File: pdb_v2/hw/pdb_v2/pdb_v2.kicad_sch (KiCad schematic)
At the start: 73 parts, among them J1 XT30-M_Ver, J2 JST-PH_01x02, J3 Conn_01x06_Pin, J5 JST-PH_01x02, J6 Conn_01x03, J7 Conn_01x03, J8 Conn_01x04, Q1 60Vds, SW1 SW_Push, SW2 SW_Push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

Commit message: changed J1 footprint
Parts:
- J1: footprint Connector_AMASS:AMASS_XT30UPB-M_1x02_P5.0mm_Vertical -> Connector_AMASS:AMASS_XT30U-M_1x02_P5.0mm_Vertical
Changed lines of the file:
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@@
 			)
 		)
-		(property "Footprint" "Connector_AMASS:AMASS_XT30UPB-M_1x02_P5.0mm_Vertical"
+		(property "Footprint" "Connector_AMASS:AMASS_XT30U-M_1x02_P5.0mm_Vertical"
 			(at 64.77 53.34 0)
 			(effects

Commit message: final changes for pcb
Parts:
- H1, H2, H3, H4: footprint MountingHole:MountingHole_2.5mm_Pad_Via -> MountingHole:MountingHole_2.5mm_Pad
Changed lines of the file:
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@@
 			)
 		)
-		(property "Footprint" "MountingHole:MountingHole_2.5mm_Pad_Via"
+		(property "Footprint" "MountingHole:MountingHole_2.5mm_Pad"
 			(at 154.94 100.33 0)
 			(effects
@@
 			)
 		)
-		(property "Footprint" "MountingHole:MountingHole_2.5mm_Pad_Via"
+		(property "Footprint" "MountingHole:MountingHole_2.5mm_Pad"
 			(at 154.94 113.03 0)
 			(effects
@@
 			)
 		)
-		(property "Footprint" "MountingHole:MountingHole_2.5mm_Pad_Via"
+		(property "Footprint" "MountingHole:MountingHole_2.5mm_Pad"
 			(at 154.94 125.73 0)
 			(effects
@@
 			)
 		)
-		(property "Footprint" "MountingHole:MountingHole_2.5mm_Pad_Via"
+		(property "Footprint" "MountingHole:MountingHole_2.5mm_Pad"
 			(at 154.94 87.63 0)
 			(effects

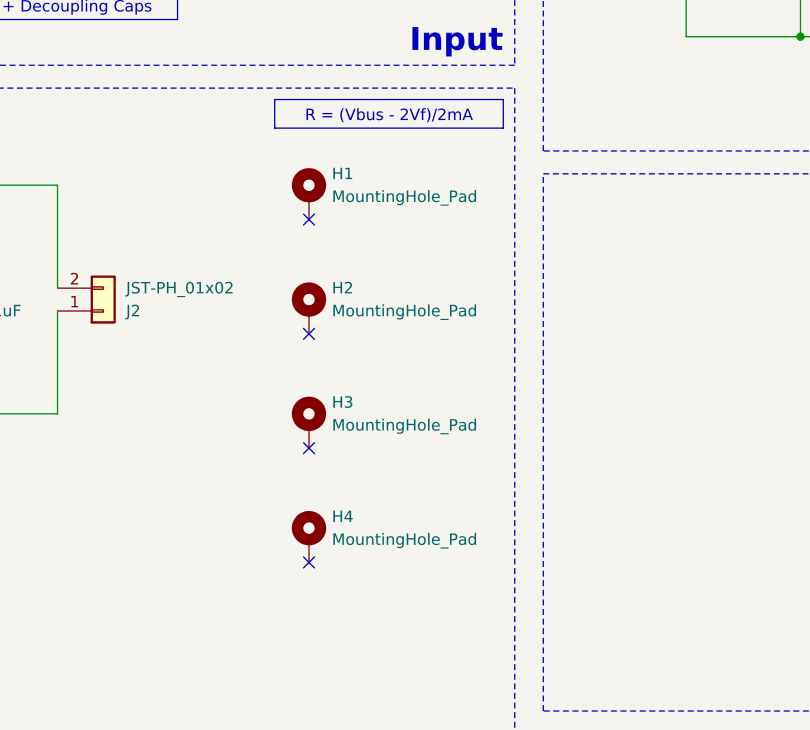
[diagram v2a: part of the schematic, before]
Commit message: removed diagonal holes
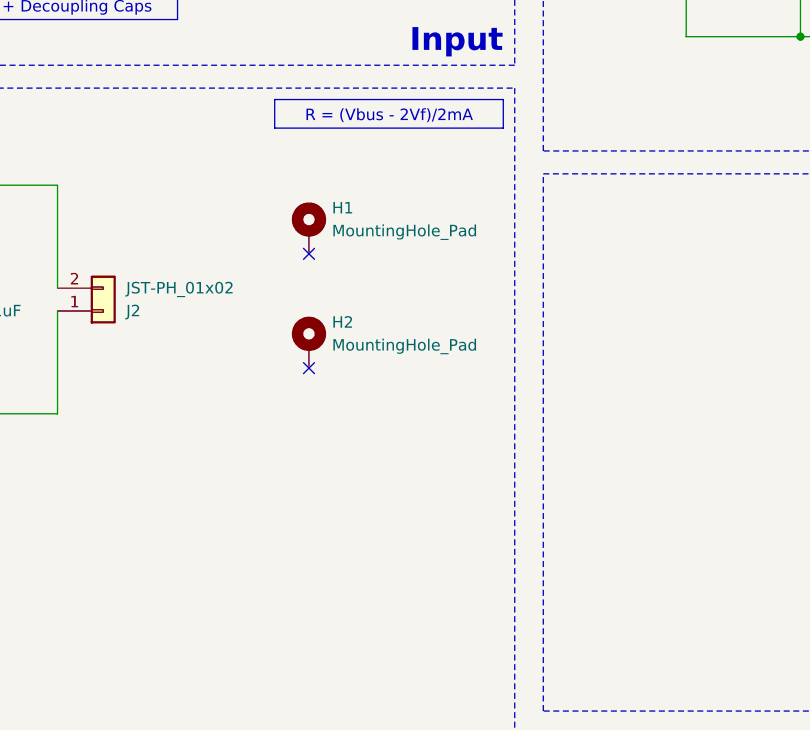
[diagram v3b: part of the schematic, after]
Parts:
- removed H1, H2: MountingHole_Pad, MountingHole:MountingHole_2.5mm_Pad, symbol Mechanical:MountingHole_Pad
- renumbered H3 to H1, H4 to H2
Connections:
- no-connect marks 26 -> 24
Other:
- moved on the sheet: H1, H2
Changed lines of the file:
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@@
 	)
 	(no_connect
-		(at 154.94 115.57)
+		(at 154.94 93.98)
 	)
 	(no_connect
@@
 	)
 	(no_connect
-		(at 154.94 102.87)
-	)
-	(no_connect
 		(at 166.37 238.76)
 	)
@@
 	)
 	(no_connect
-		(at 154.94 90.17)
-	)
-	(no_connect
 		(at 166.37 243.84)
 	)
@@
 	)
 	(no_connect
-		(at 154.94 128.27)
+		(at 154.94 106.68)
 	)
 	(no_connect
@@
 	)
 	(symbol
-		(lib_id "Mechanical:MountingHole_Pad")
-		(at 154.94 100.33 0)
-		(unit 1)
-		(exclude_from_sim no)
-		(in_bom no)
-		(on_board yes)
-		(dnp no)
-		(fields_autoplaced yes)
-		(property "Reference" "H2"
-			(at 157.48 97.7899 0)
-			(effects
-				(font
-					(size 1.27 1.27)
-				)
-				(justify left)
-			)
-		)
-		(property "Value" "MountingHole_Pad"
-			(at 157.48 100.3299 0)
-			(effects
-				(font
-					(size 1.27 1.27)
-				)
-				(justify left)
-			)
-		)
-		(property "Footprint" "MountingHole:MountingHole_2.5mm_Pad"
-			(at 154.94 100.33 0)
-			(effects
-				(font
-					(size 1.27 1.27)
-				)
-				(hide yes)
-			)
-		)
-		(property "Datasheet" ""
-			(at 154.94 100.33 0)
-			(effects
-				(font
-					(size 1.27 1.27)
-				)
-				(hide yes)
-			)
-		)
-		(property "Description" ""
-			(at 154.94 100.33 0)
-			(effects
-				(font
-					(size 1.27 1.27)
-				)
-				(hide yes)
-			)
-		)
-		(pin "1"
-		)
-		(instances
-			(project "power_distribution"
-				(path "/60722063-abcd-445d-bfe3-2bc3b4deef0d"
-					(reference "H2")
-					(unit 1)
-				)
-			)
-		)
-	)
-	(symbol
 		(lib_id "Device:C")
 		(at 228.6 125.73 0)
@@
 	(symbol
 		(lib_id "Mechanical:MountingHole_Pad")
-		(at 154.94 113.03 0)
+		(at 154.94 91.44 0)
 		(unit 1)
 		(exclude_from_sim no)
@@
 		(dnp no)
 		(fields_autoplaced yes)
-		(property "Reference" "H3"
-			(at 157.48 110.4899 0)
+		(property "Reference" "H1"
+			(at 157.48 88.8999 0)
 			(effects
 				(font
@@
 		)
 		(property "Value" "MountingHole_Pad"
-			(at 157.48 113.0299 0)
+			(at 157.48 91.4399 0)
 			(effects
 				(font
@@
 		)
 		(property "Footprint" "MountingHole:MountingHole_2.5mm_Pad"
-			(at 154.94 113.03 0)
+			(at 154.94 91.44 0)
 			(effects
 				(font
@@
 		)
 		(property "Datasheet" ""
-			(at 154.94 113.03 0)
+			(at 154.94 91.44 0)
 			(effects
 				(font
@@
 		)
 		(property "Description" ""
-			(at 154.94 113.03 0)
+			(at 154.94 91.44 0)
 			(effects
 				(font
@@
 			(project "power_distribution"
 				(path "/60722063-abcd-445d-bfe3-2bc3b4deef0d"
-					(reference "H3")
+					(reference "H1")
 					(unit 1)
 				)
@@
 	(symbol
 		(lib_id "Mechanical:MountingHole_Pad")
-		(at 154.94 125.73 0)
+		(at 154.94 104.14 0)
 		(unit 1)
 		(exclude_from_sim no)
@@
 		(dnp no)
 		(fields_autoplaced yes)
-		(property "Reference" "H4"
-			(at 157.48 123.1899 0)
+		(property "Reference" "H2"
+			(at 157.48 101.5999 0)
 			(effects
 				(font
@@
 		)
 		(property "Value" "MountingHole_Pad"
-			(at 157.48 125.7299 0)
+			(at 157.48 104.1399 0)
 			(effects
 				(font
@@
 		)
 		(property "Footprint" "MountingHole:MountingHole_2.5mm_Pad"
-			(at 154.94 125.73 0)
+			(at 154.94 104.14 0)
 			(effects
 				(font
@@
 		)
 		(property "Datasheet" ""
-			(at 154.94 125.73 0)
+			(at 154.94 104.14 0)
 			(effects
 				(font
@@
 		)
 		(property "Description" ""
-			(at 154.94 125.73 0)
+			(at 154.94 104.14 0)
 			(effects
 				(font
@@
 			(project "power_distribution"
 				(path "/60722063-abcd-445d-bfe3-2bc3b4deef0d"
-					(reference "H4")
+					(reference "H2")
 					(unit 1)
 				)
@@
 					(unit 1)
 				)
-			)
-		)
-	)
-	(symbol
-		(lib_id "Mechanical:MountingHole_Pad")
-		(at 154.94 87.63 0)
-		(unit 1)
-		(exclude_from_sim no)
-		(in_bom no)
-		(on_board yes)
-		(dnp no)
-		(property "Reference" "H1"
-			(at 157.48 85.0899 0)
-			(effects
-				(font
-					(size 1.27 1.27)
-				)
-				(justify left)
-			)
-		)
-		(property "Value" "MountingHole_Pad"
-			(at 157.48 87.6299 0)
-			(effects
-				(font
-					(size 1.27 1.27)
-				)
-				(justify left)
-			)
-		)
-		(property "Footprint" "MountingHole:MountingHole_2.5mm_Pad"
-			(at 154.94 87.63 0)
-			(effects
-				(font
-					(size 1.27 1.27)
-				)
-				(hide yes)
-			)
-		)
-		(property "Datasheet" ""
-			(at 154.94 87.63 0)
-			(effects
-				(font
-					(size 1.27 1.27)
-				)
-				(hide yes)
-			)
-		)
-		(property "Description" ""
-			(at 154.94 87.63 0)
-			(effects
-				(font
-					(size 1.27 1.27)
-				)
-				(hide yes)
-			)
-		)
-		(pin "1"
-		)
-		(instances
-			(project ""
-				(path "/60722063-abcd-445d-bfe3-2bc3b4deef0d"
-					(reference "H1")
-					(unit 1)
-				)

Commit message: improved
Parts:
- SW1, SW2: footprint Button_Switch_SMD:SW_SPST_TL3342 -> Button_Switch_THT:SW_PUSH_6mm
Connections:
- net 3V3_BUS: no longer R9.1
- net LED: now reaches U2.30 (IO18)
- net LED: now also R9.1
- no-connect marks 24 -> 23
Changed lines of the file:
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@@
 	)
 	(no_connect
-		(at 196.85 233.68)
-	)
-	(no_connect
 		(at 154.94 93.98)
 	)
@@
 	(wire
 		(pts
+			(xy 196.85 233.68) (xy 208.28 233.68)
+		)
+		(stroke
+			(width 0)
+			(type default)
+		)
+	)
+	(wire
+		(pts
 			(xy 292.1 38.1) (xy 292.1 49.53)
 		)
@@
 	(wire
 		(pts
-			(xy 191.77 184.15) (xy 193.04 184.15)
-		)
-		(stroke
-			(width 0)
-			(type default)
-		)
-	)
-	(wire
-		(pts
 			(xy 40.64 241.3) (xy 52.07 241.3)
 		)
@@
 	(wire
 		(pts
+			(xy 187.96 184.15) (xy 193.04 184.15)
+		)
+		(stroke
+			(width 0)
+			(type default)
+		)
+	)
+	(wire
+		(pts
 			(xy 115.57 201.93) (xy 116.84 201.93)
 		)
@@
 		)
 	)
+	(label "LED"
+		(at 187.96 184.15 0)
+		(effects
+			(font
+				(size 1.27 1.27)
+			)
+			(justify left bottom)
+		)
+	)
 	(label "3V3_SPLIT"
 		(at 67.31 127 90)
@@
 		)
 	)
+	(label "LED"
+		(at 208.28 233.68 180)
+		(effects
+			(font
+				(size 1.27 1.27)
+			)
+			(justify right bottom)
+		)
+	)
 	(label "3V3_SPLIT"
 		(at 50.8 139.7 0)
@@
 		)
 	)
-	(global_label "3V3_BUS"
-		(shape input)
-		(at 191.77 184.15 180)
-		(fields_autoplaced yes)
-		(effects
-			(font
-				(size 1.27 1.27)
-			)
-			(justify right)
-		)
-		(property "Intersheetrefs" "${INTERSHEET_REFS}"
-			(at 180.4996 184.15 0)
-			(effects
-				(font
-					(size 1.27 1.27)
-				)
-				(justify right)
-				(hide yes)
-			)
-		)
-	)
 	(global_label "12V_BUS"
 		(shape output)
@@
 			)
 		)
-		(property "Footprint" "Button_Switch_SMD:SW_SPST_TL3342"
+		(property "Footprint" "Button_Switch_THT:SW_PUSH_6mm"
 			(at 120.65 196.85 0)
 			(effects
@@
 			)
 		)
-		(property "Footprint" "Button_Switch_SMD:SW_SPST_TL3342"
+		(property "Footprint" "Button_Switch_THT:SW_PUSH_6mm"
 			(at 86.36 198.12 0)
 			(effects

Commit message: Sent to Matthew for review
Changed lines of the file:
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@@
-	)
-	(junction
-		(at 81.28 203.2)
-		(diameter 0)
-		(color 0 0 0 0)
 	)
 	(junction
@@
 	)
 	(junction
-		(at 115.57 201.93)
-		(diameter 0)
-		(color 0 0 0 0)
-	)
-	(junction
 		(at 129.54 201.93)
 		(diameter 0)
@@
 	(wire
 		(pts
-			(xy 81.28 203.2) (xy 82.55 203.2)
-		)
-		(stroke
-			(width 0)
-			(type default)
-		)
-	)
-	(wire
-		(pts
 			(xy 331.47 38.1) (xy 331.47 46.99)
 		)
@@
 		)
 		(stroke
-			(width 0)
-			(type default)
-		)
-	)
-	(wire
-		(pts
-			(xy 115.57 201.93) (xy 116.84 201.93)
-		)
-		(stroke

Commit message: Zipped up gerber + drill files!
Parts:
- removed GND2: GND, test_point_custom:TestPoint_Pad_D1.0mm, symbol Connector:TestPoint
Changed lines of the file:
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@@
 	)
 	(junction
-		(at 279.4 59.69)
-		(diameter 0)
-		(color 0 0 0 0)
-	)
-	(junction
 		(at 318.77 38.1)
 		(diameter 0)
@@
 					(unit 1)
 				)
-			)
-		)
-	)
-	(symbol
-		(lib_id "Connector:TestPoint")
-		(at 279.4 59.69 270)
-		(unit 1)
-		(exclude_from_sim no)
-		(in_bom yes)
-		(on_board yes)
-		(dnp no)
-		(fields_autoplaced yes)
-		(property "Reference" "GND2"
-			(at 284.48 58.4199 90)
-			(effects
-				(font
-					(size 1.27 1.27)
-				)
-				(justify left)
-				(hide yes)
-			)
-		)
-		(property "Value" "GND"
-			(at 284.48 60.9599 90)
-			(effects
-				(font
-					(size 1.27 1.27)
-				)
-				(justify left)
-			)
-		)
-		(property "Footprint" "test_point_custom:TestPoint_Pad_D1.0mm"
-			(at 279.4 64.77 0)
-			(effects
-				(font
-					(size 1.27 1.27)
-				)
-				(hide yes)
-			)
-		)
-		(property "Datasheet" "~"
-			(at 279.4 64.77 0)
-			(effects
-				(font
-					(size 1.27 1.27)
-				)
-				(hide yes)
-			)
-		)
-		(property "Description" "test point"
-			(at 279.4 59.69 0)
-			(effects
-				(font
-					(size 1.27 1.27)
-				)
-				(hide yes)
-			)
-		)
-		(pin "1"
-		)
-		(instances
-			(project "power_distribution"
-				(path "/60722063-abcd-445d-bfe3-2bc3b4deef0d"
-					(reference "GND2")
-					(unit 1)
-				)
